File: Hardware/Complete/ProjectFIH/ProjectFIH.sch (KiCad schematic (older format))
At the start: 85 parts, among them J1 Conn_01x02_Male, J10 Payload LED, J2 Power, J3 Power LED, J4 MCU Fail LED, J5 Heater LED, J6 Heater, J7 UART, J8 AVR-ISP-10, J9 Payload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

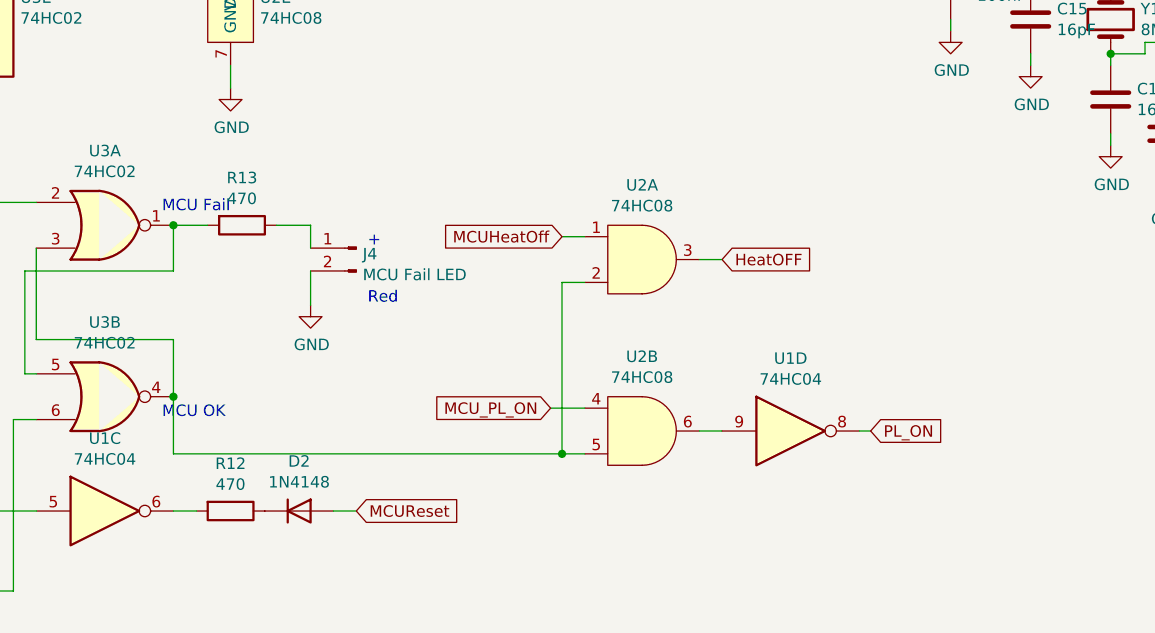
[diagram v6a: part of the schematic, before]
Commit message: Swapped outputs of U3
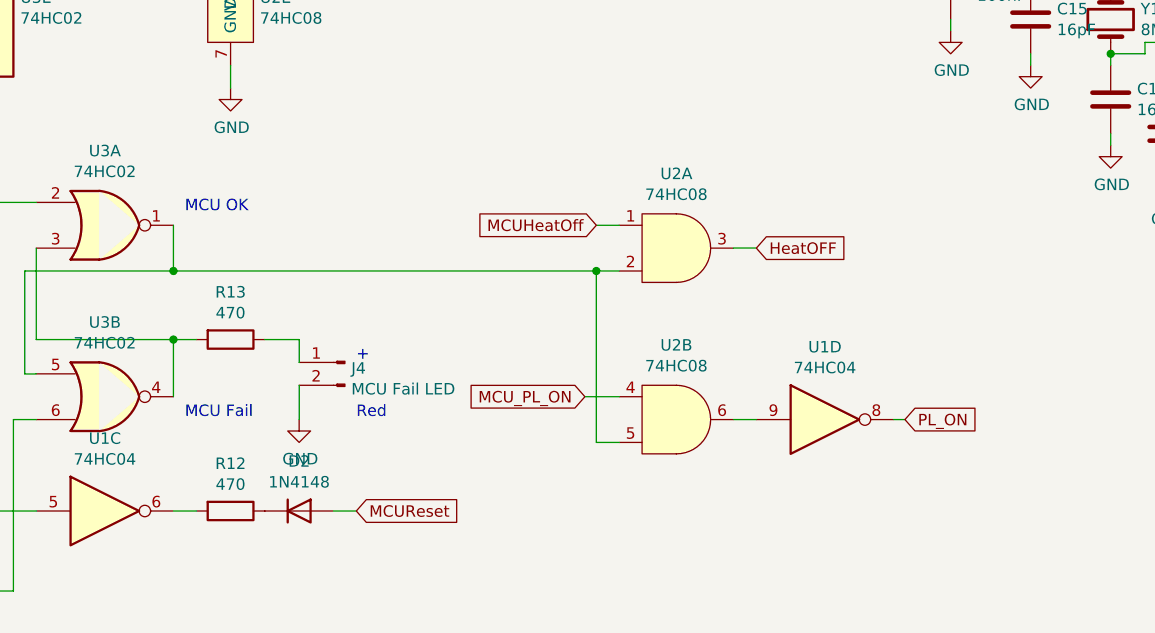
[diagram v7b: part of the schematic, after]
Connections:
- net at U3.1, U3.5: now also U2.2, U2.5; no longer R13.2
- net at U3.3, U3.4: now also R13.2; no longer U2.2, U2.5
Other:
- moved on the sheet: J4, R13, U1D, U2A, U2B
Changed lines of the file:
@@
 Wire Wire Line
 	4650 6900 4700 6900
-Text Notes 5250 6200 0    50   ~ 0
+Text Notes 5350 7100 0    50   ~ 0
 MCU Fail
-Text Notes 5250 7100 0    50   ~ 0
+Text Notes 5350 6200 0    50   ~ 0
 MCU OK
 Wire Wire Line
@@
 L 74xx:74HC04 U1
 U 4 1 5F1DCE8A
-P 8000 7150
-F 0 "U1" H 8000 7467 50  0000 C CNN
-F 1 "74HC04" H 8000 7376 50  0000 C CNN
-F 2 "Package_SO:SOIC-14_3.9x8.7mm_P1.27mm" H 8000 7150 50  0001 C CNN
-F 3 "https://assets.nexperia.com/documents/data-sheet/74HC_HCT04.pdf" H 8000 7150 50  0001 C CNN
-	4    8000 7150
+P 8150 7100
+F 0 "U1" H 8150 7417 50  0000 C CNN
+F 1 "74HC04" H 8150 7326 50  0000 C CNN
+F 2 "Package_SO:SOIC-14_3.9x8.7mm_P1.27mm" H 8150 7100 50  0001 C CNN
+F 3 "https://assets.nexperia.com/documents/data-sheet/74HC_HCT04.pdf" H 8150 7100 50  0001 C CNN
+	4    8150 7100
 	1    0    0    -1
 $EndComp
@@
 L Device:R R13
 U 1 1 5F0ECE76
-P 5600 6250
-F 0 "R13" V 5393 6250 50  0000 C CNN
-F 1 "470" V 5484 6250 50  0000 C CNN
-F 2 "Resistor_SMD:R_0805_2012Metric_Pad1.15x1.40mm_HandSolder" V 5530 6250 50  0001 C CNN
-F 3 "~" H 5600 6250 50  0001 C CNN
-	1    5600 6250
+P 5550 6750
+F 0 "R13" V 5343 6750 50  0000 C CNN
+F 1 "470" V 5434 6750 50  0000 C CNN
+F 2 "Resistor_SMD:R_0805_2012Metric_Pad1.15x1.40mm_HandSolder" V 5480 6750 50  0001 C CNN
+F 3 "~" H 5550 6750 50  0001 C CNN
+	1    5550 6750
 	0    1    1    0
 $EndComp
 Wire Wire Line
-	5450 6250 5300 6250
-Connection ~ 5300 6250
-Wire Wire Line
-	5900 6250 5750 6250
+	5850 6750 5700 6750
 $Comp
 L power:GND #PWR036
 U 1 1 5F1376C2
-P 5900 6600
-F 0 "#PWR036" H 5900 6350 50  0001 C CNN
-F 1 "GND" H 5905 6427 50  0000 C CNN
-F 2 "" H 5900 6600 50  0001 C CNN
-F 3 "" H 5900 6600 50  0001 C CNN
-	1    5900 6600
+P 5850 7100
+F 0 "#PWR036" H 5850 6850 50  0001 C CNN
+F 1 "GND" H 5855 6927 50  0000 C CNN
+F 2 "" H 5850 7100 50  0001 C CNN
+F 3 "" H 5850 7100 50  0001 C CNN
+	1    5850 7100
 	1    0    0    -1
 $EndComp
@@
 L Fossa_library:74HC08 U2
 U 1 1 5F18724F
-P 7300 6200
-F 0 "U2" H 7350 6325 50  0000 C CNN
-F 1 "74HC08" H 7350 6234 50  0000 C CNN
-F 2 "Package_SO:SOIC-14_3.9x8.7mm_P1.27mm" H 7300 6200 50  0001 C CNN
-F 3 "" H 7300 6200 50  0001 C CNN
-	1    7300 6200
+P 7450 6150
+F 0 "U2" H 7500 6275 50  0000 C CNN
+F 1 "74HC08" H 7500 6184 50  0000 C CNN
+F 2 "Package_SO:SOIC-14_3.9x8.7mm_P1.27mm" H 7450 6150 50  0001 C CNN
+F 3 "" H 7450 6150 50  0001 C CNN
+	1    7450 6150
 	1    0    0    -1
 $EndComp
@@
 L Fossa_library:74HC08 U2
 U 2 1 5F189EAD
-P 7300 6950
-F 0 "U2" H 7350 7075 50  0000 C CNN
-F 1 "74HC08" H 7350 6984 50  0000 C CNN
-F 2 "Package_SO:SOIC-14_3.9x8.7mm_P1.27mm" H 7300 6950 50  0001 C CNN
-F 3 "" H 7300 6950 50  0001 C CNN
-	2    7300 6950
-	1    0    0    -1
-$EndComp
-Wire Wire Line
-	7100 6500 7000 6500
-Wire Wire Line
-	7000 6500 7000 7250
-Wire Wire Line
-	7000 7250 7100 7250
-Wire Wire Line
-	7000 7250 5300 7250
-Wire Wire Line
-	5300 7250 5300 7000
-Connection ~ 7000 7250
-Connection ~ 5300 7000
-Text GLabel 7000 6300 0    50   Input ~ 0
+P 7450 6900
+F 0 "U2" H 7500 7025 50  0000 C CNN
+F 1 "74HC08" H 7500 6934 50  0000 C CNN
+F 2 "Package_SO:SOIC-14_3.9x8.7mm_P1.27mm" H 7450 6900 50  0001 C CNN
+F 3 "" H 7450 6900 50  0001 C CNN
+	2    7450 6900
+	1    0    0    -1
+$EndComp
+Wire Wire Line
+	7250 6450 7150 6450
+Wire Wire Line
+	7150 6450 7150 7200
+Wire Wire Line
+	7150 7200 7250 7200
+Text GLabel 7150 6250 0    50   Input ~ 0
 MCUHeatOff
 Wire Wire Line
-	7100 6300 7000 6300
-Text GLabel 7700 6400 2    50   Input ~ 0
+	7250 6250 7150 6250
+Text GLabel 7850 6350 2    50   Input ~ 0
 HeatOFF
 Wire Wire Line
-	7700 6400 7600 6400
-Text GLabel 6950 7050 0    50   Input ~ 0
+	7850 6350 7750 6350
+Text GLabel 7100 7000 0    50   Input ~ 0
 MCU_PL_ON
 Wire Wire Line
-	6950 7050 7100 7050
-Text GLabel 8350 7150 2    50   Input ~ 0
+	7100 7000 7250 7000
+Text GLabel 8500 7100 2    50   Input ~ 0
 PL_ON
 Wire Wire Line
-	7700 7150 7600 7150
+	7850 7100 7750 7100
 $Comp
 L Fossa_library:74HC08 U2
@@
 $EndComp
 Wire Wire Line
-	8350 7150 8300 7150
+	8500 7100 8450 7100
 Wire Wire Line
 	2750 6500 2950 6500
@@
 L Connector:Conn_01x02_Male J4
 U 1 1 5F18621B
-P 6100 6350
-F 0 "J4" H 6072 6324 50  0000 R CNN
-F 1 "MCU Fail LED" H 6072 6233 50  0000 R CNN
-F 2 "Connector_PinHeader_2.54mm:PinHeader_1x02_P2.54mm_Vertical" H 6100 6350 50  0001 C CNN
-F 3 "~" H 6100 6350 50  0001 C CNN
-	1    6100 6350
+P 6050 6850
+F 0 "J4" H 6022 6824 50  0000 R CNN
+F 1 "MCU Fail LED" H 6022 6733 50  0000 R CNN
+F 2 "Connector_PinHeader_2.54mm:PinHeader_1x02_P2.54mm_Vertical" H 6050 6850 50  0001 C CNN
+F 3 "~" H 6050 6850 50  0001 C CNN
+	1    6050 6850
 	-1   0    0    -1
 $EndComp
 Wire Wire Line
-	5900 6250 5900 6350
-Wire Wire Line
-	5900 6450 5900 6600
-Text Notes 6150 6350 0    50   ~ 0
+	5850 6750 5850 6850
+Wire Wire Line
+	5850 6950 5850 7100
+Text Notes 6100 6850 0    50   ~ 0
 +
-Text Notes 6150 6600 0    50   ~ 0
+Text Notes 6100 7100 0    50   ~ 0
 Red
 $Comp
@@
 Wire Wire Line
 	11550 6650 11500 6650
+Wire Wire Line
+	5400 6750 5300 6750
+Connection ~ 5300 6750
+Connection ~ 7150 6450
+Wire Wire Line
+	5300 6450 7150 6450
+Connection ~ 5300 6450
 $EndSCHEMATC

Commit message: Early firmware development.
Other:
- note added: "White"
- note removed: "Orange"
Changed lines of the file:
@@
 +
 Text Notes 7700 2250 0    50   ~ 0
-Orange
+White
 Wire Wire Line
 	7450 2450 7450 2550
